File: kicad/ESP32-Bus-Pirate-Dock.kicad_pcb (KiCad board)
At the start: 4 copper layers, 80 x 73.8 mm, 39 parts, among them CN1 HX25418-10WA, J1 Conn_01x10V, J2 Conn_01x22, J3 Conn_01x22, J4 Conn_02x03, J5 Conn_01x22, J6 Conn_01x22, J7 Conn_01x22, Q2 2N7002, SW1 TA-3532S-A2, U2 TS5A3157DBVR, U3 TMUX1574PW, U4 TLV75518PDBV, U7 TMUX1574PW, U8 TXS0108EPW, U9 TXS0108EPW

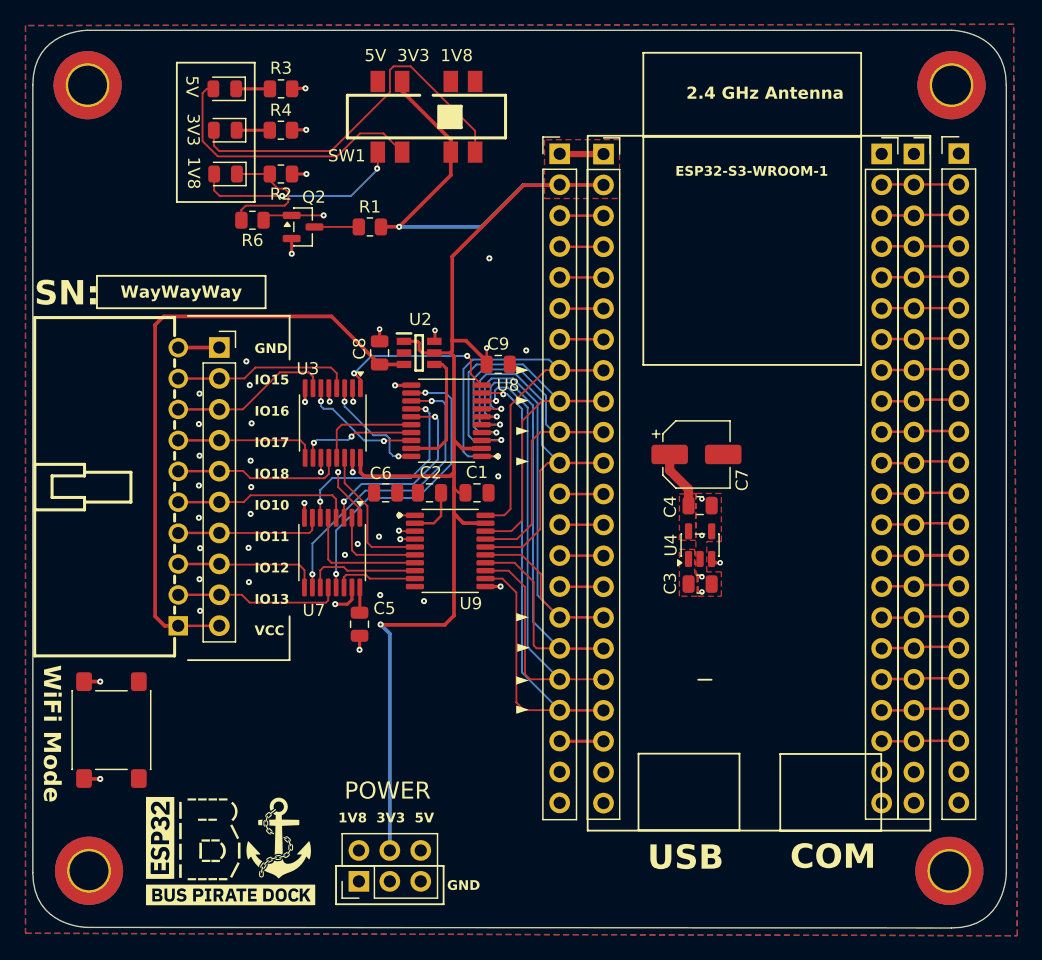
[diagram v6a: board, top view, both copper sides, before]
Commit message: Connected PCB
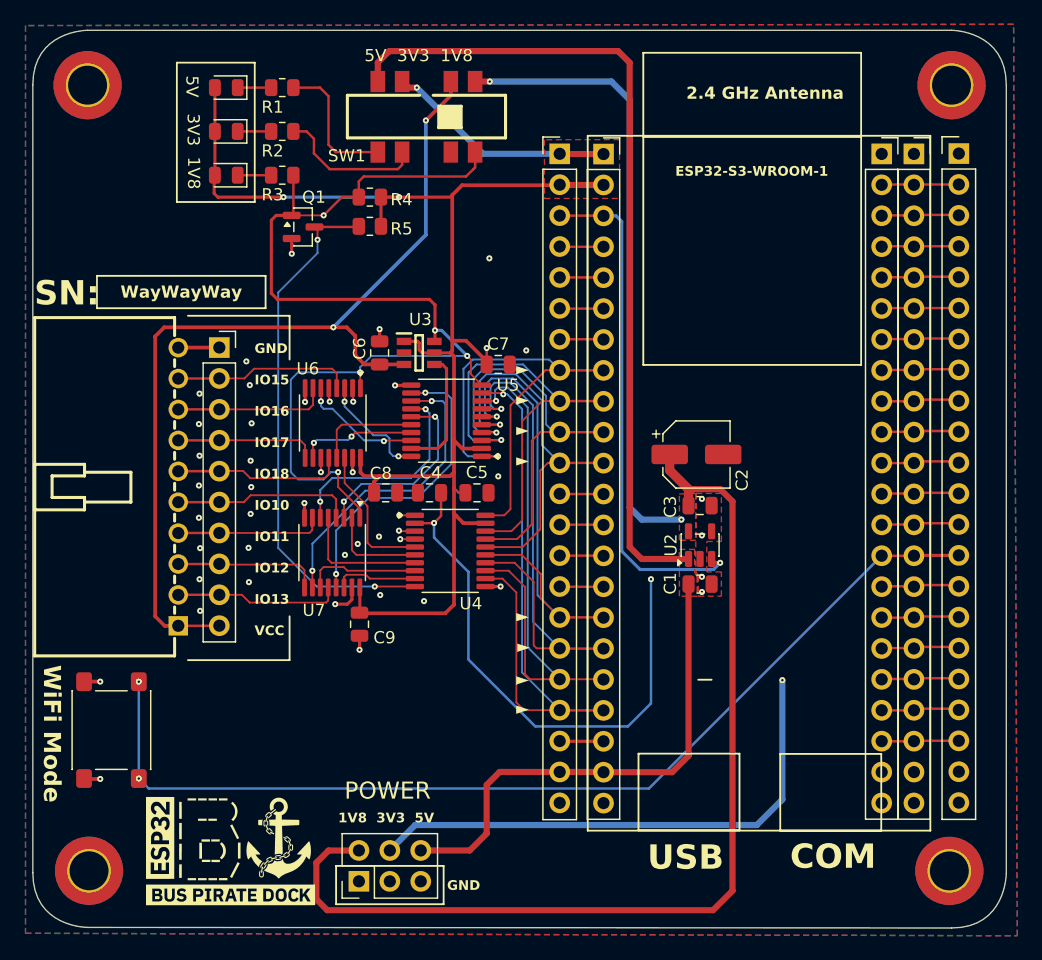
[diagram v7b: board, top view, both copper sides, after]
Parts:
- moved R4 7.56 mm to (151.4, 74.0), turned to 0 degrees
- moved R3 4.44 mm to (144.2, 72.2)
- moved D2 3.50 mm to (139.6, 68.6)
- moved R1 3.50 mm to (144.2, 65.0)
- moved R2 3.50 mm to (144.2, 68.6)
- moved D1 3.50 mm to (139.6, 65.0)
- moved D3 0.12 mm to (139.6, 72.2)
- renumbered C3 to C1, C7 to C2, C4 to C3, C2 to C4, C1 to C5, C8 to C6, C9 to C7, C6 to C8, C5 to C9, D3 to D1, D1 to D3, H4 to H1, H3 to H2, H2 to H3, H1 to H4, J6 to J1, J3 to J2, J1 to J3, J2 to J4, J7 to J6, J4 to J7, Q2 to Q1, R4 to R1, R3 to R2, R6 to R3, R2 to R4, R1 to R5, U4 to U2, U2 to U3, U9 to U4, U8 to U5, U3 to U6
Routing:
- net +1V8: track 9.14 -> 185.6 mm, vias 0 -> 4
- net +5V: track 0.00 -> 109.8 mm
- net GPIO0: track 6.36 -> 83.6 mm, vias 0 -> 2
- net +3.3V: track 173.1 -> 234.0 mm
- net /Voltage Level Translator/~{SEL}: track 3.64 -> 44.0 mm, vias 0 -> 2
- net RST: track 4.68 -> 42.4 mm
- net (no net): track 30.8 -> 0.00 mm
- net /Voltage Level Translator/SEL: track 57.1 -> 86.5 mm, vias 6 -> 5
- net VTARGET: track 51.9 -> 75.9 mm, vias 0 -> 2
- net /Voltage Level Translator/3V3_SEL: track 1.20 -> 12.1 mm, vias 1 -> 0
- net /Voltage Level Translator/5V_SEL: track 1.20 -> 11.5 mm, vias 1 -> 0
- net /Voltage Level Translator/D1_K: track 10.9 -> 2.75 mm
- net IO16: track 13.4 -> 12.6 mm
